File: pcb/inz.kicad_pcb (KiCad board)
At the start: 2 copper layers, 410 parts, among them U1 AMS1117-3.3, U2 ESP32-S3-WROOM-1

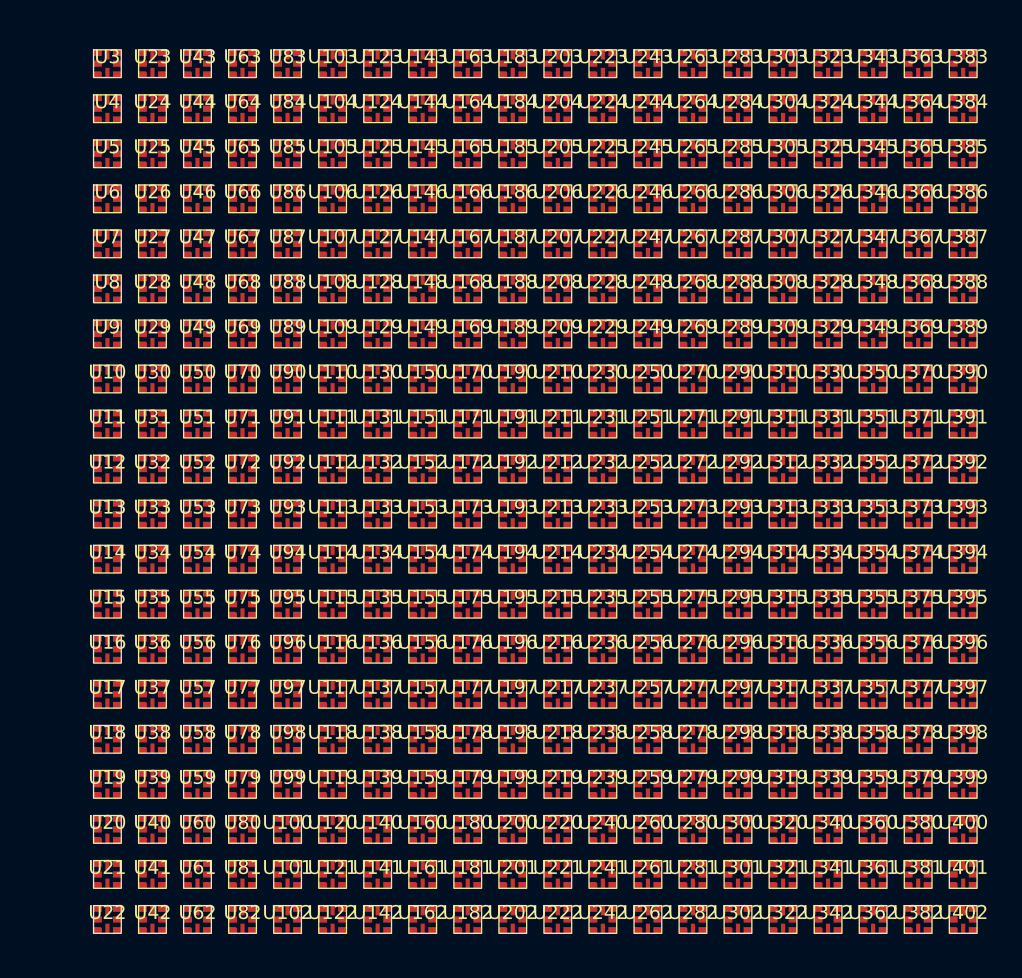
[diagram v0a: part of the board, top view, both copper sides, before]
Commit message: Fixed Led alignment in the pcb project
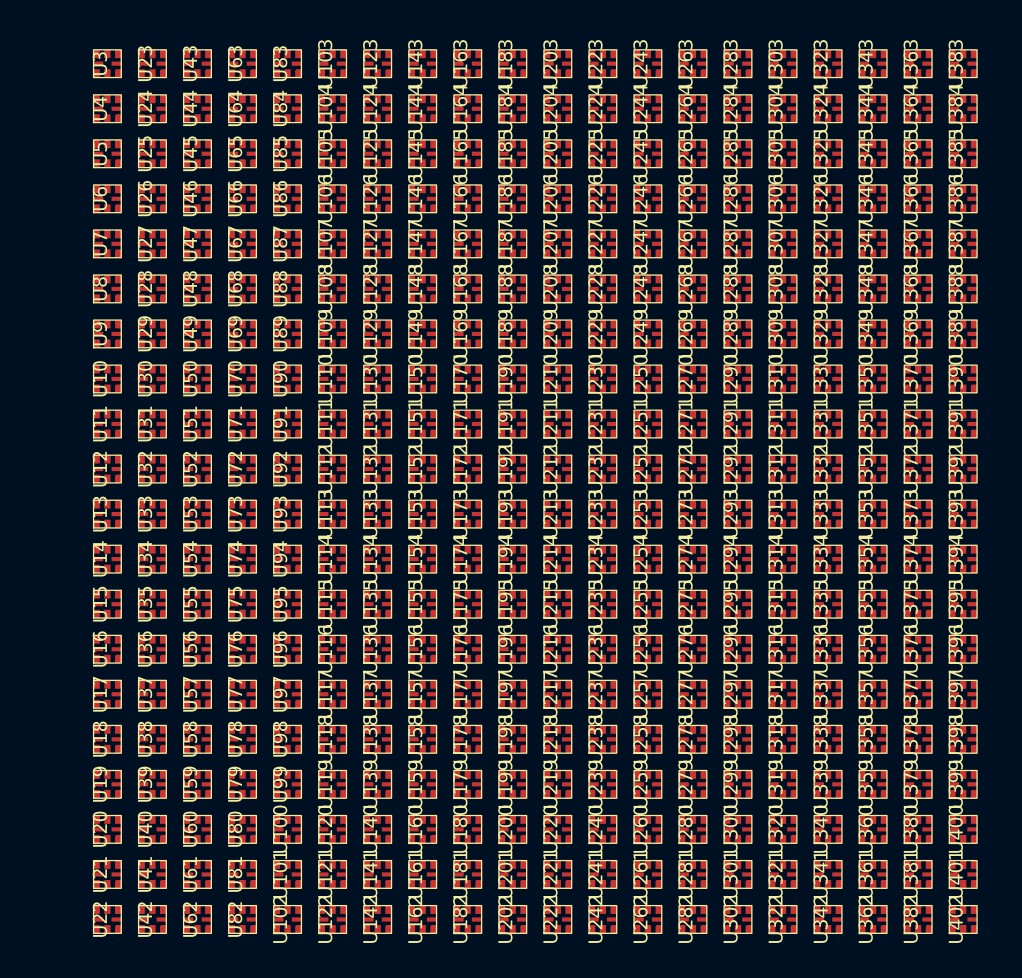
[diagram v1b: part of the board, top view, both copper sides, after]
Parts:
- turned U10 to 90 degrees
- turned U100 to 90 degrees
- turned U101 to 90 degrees
- turned U102 to 90 degrees
- turned U103 to 90 degrees
- turned U104 to 90 degrees
- turned U105 to 90 degrees
- turned U106 to 90 degrees
- turned U107 to 90 degrees
- turned U108 to 90 degrees
- turned U109 to 90 degrees
- turned U11 to 90 degrees
- turned U110 to 90 degrees
- turned U111 to 90 degrees
- turned U112 to 90 degrees
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
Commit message: pcb update
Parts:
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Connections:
- U103 pad 3: Net-(U103-CLI) -> Net-(U102-CLO)
- U103 pad 6: Net-(U103-DAI) -> Net-(U102-DAO)
- U104 pad 1: Net-(U103-CLI) -> Net-(U104-CLO)
- U104 pad 3: Net-(U104-CLI) -> Net-(U103-CLO)
- U104 pad 4: Net-(U103-DAI) -> Net-(U104-DAO)
- U104 pad 6: Net-(U104-DAI) -> Net-(U103-DAO)
- U105 pad 1: Net-(U104-CLI) -> Net-(U105-CLO)
- U105 pad 3: Net-(U105-CLI) -> Net-(U104-CLO)
- U105 pad 4: Net-(U104-DAI) -> Net-(U105-DAO)
- U105 pad 6: Net-(U105-DAI) -> Net-(U104-DAO)
- U106 pad 1: Net-(U105-CLI) -> Net-(U106-CLO)
- U106 pad 3: Net-(U106-CLI) -> Net-(U105-CLO)
- U106 pad 4: Net-(U105-DAI) -> Net-(U106-DAO)
- U106 pad 6: Net-(U106-DAI) -> Net-(U105-DAO)
- U107 pad 1: Net-(U106-CLI) -> Net-(U107-CLO)
- U107 pad 3: Net-(U107-CLI) -> Net-(U106-CLO)
- U107 pad 4: Net-(U106-DAI) -> Net-(U107-DAO)
- U107 pad 6: Net-(U107-DAI) -> Net-(U106-DAO)
- U108 pad 1: Net-(U107-CLI) -> Net-(U108-CLO)
- U108 pad 3: Net-(U108-CLI) -> Net-(U107-CLO)
- U108 pad 4: Net-(U107-DAI) -> Net-(U108-DAO)
- U108 pad 6: Net-(U108-DAI) -> Net-(U107-DAO)
- U109 pad 1: Net-(U108-CLI) -> Net-(U109-CLO)
- U109 pad 3: Net-(U109-CLI) -> Net-(U108-CLO)
- U109 pad 4: Net-(U108-DAI) -> Net-(U109-DAO)
- U109 pad 6: Net-(U109-DAI) -> Net-(U108-DAO)
- U110 pad 1: Net-(U109-CLI) -> Net-(U110-CLO)
- U110 pad 3: Net-(U110-CLI) -> Net-(U109-CLO)
- U110 pad 4: Net-(U109-DAI) -> Net-(U110-DAO)
- U110 pad 6: Net-(U110-DAI) -> Net-(U109-DAO)
- U111 pad 1: Net-(U110-CLI) -> Net-(U111-CLO)
- U111 pad 3: Net-(U111-CLI) -> Net-(U110-CLO)
- U111 pad 4: Net-(U110-DAI) -> Net-(U111-DAO)
- U111 pad 6: Net-(U111-DAI) -> Net-(U110-DAO)
- U112 pad 1: Net-(U111-CLI) -> Net-(U112-CLO)
- U112 pad 3: Net-(U112-CLI) -> Net-(U111-CLO)
- U112 pad 4: Net-(U111-DAI) -> Net-(U112-DAO)
- U112 pad 6: Net-(U112-DAI) -> Net-(U111-DAO)
- U113 pad 1: Net-(U112-CLI) -> Net-(U113-CLO)
- U113 pad 3: Net-(U113-CLI) -> Net-(U112-CLO)
- U113 pad 4: Net-(U112-DAI) -> Net-(U113-DAO)
- U113 pad 6: Net-(U113-DAI) -> Net-(U112-DAO)
- U114 pad 1: Net-(U113-CLI) -> Net-(U114-CLO)
- U114 pad 3: Net-(U114-CLI) -> Net-(U113-CLO)
- U114 pad 4: Net-(U113-DAI) -> Net-(U114-DAO)
- U114 pad 6: Net-(U114-DAI) -> Net-(U113-DAO)
- U115 pad 1: Net-(U114-CLI) -> Net-(U115-CLO)
- U115 pad 3: Net-(U115-CLI) -> Net-(U114-CLO)
- U115 pad 4: Net-(U114-DAI) -> Net-(U115-DAO)
- U115 pad 6: Net-(U115-DAI) -> Net-(U114-DAO)
- U116 pad 1: Net-(U115-CLI) -> Net-(U116-CLO)
- U116 pad 3: Net-(U116-CLI) -> Net-(U115-CLO)
- U116 pad 4: Net-(U115-DAI) -> Net-(U116-DAO)
- U116 pad 6: Net-(U116-DAI) -> Net-(U115-DAO)
- U117 pad 1: Net-(U116-CLI) -> Net-(U117-CLO)
- U117 pad 3: Net-(U117-CLI) -> Net-(U116-CLO)
- U117 pad 4: Net-(U116-DAI) -> Net-(U117-DAO)
- U117 pad 6: Net-(U117-DAI) -> Net-(U116-DAO)
- U118 pad 1: Net-(U117-CLI) -> Net-(U118-CLO)
- U118 pad 3: Net-(U118-CLI) -> Net-(U117-CLO)
- U118 pad 4: Net-(U117-DAI) -> Net-(U118-DAO)
- U118 pad 6: Net-(U118-DAI) -> Net-(U117-DAO)
- U119 pad 1: Net-(U118-CLI) -> Net-(U119-CLO)
- U119 pad 3: Net-(U119-CLI) -> Net-(U118-CLO)
- U119 pad 4: Net-(U118-DAI) -> Net-(U119-DAO)
- U119 pad 6: Net-(U119-DAI) -> Net-(U118-DAO)
- U120 pad 1: Net-(U119-CLI) -> Net-(U120-CLO)
- U120 pad 3: Net-(U120-CLI) -> Net-(U119-CLO)
- U120 pad 4: Net-(U119-DAI) -> Net-(U120-DAO)
- U120 pad 6: Net-(U120-DAI) -> Net-(U119-DAO)
- U121 pad 1: Net-(U120-CLI) -> Net-(U121-CLO)
- U121 pad 3: Net-(U121-CLI) -> Net-(U120-CLO)
- U121 pad 4: Net-(U120-DAI) -> Net-(U121-DAO)
- U121 pad 6: Net-(U121-DAI) -> Net-(U120-DAO)
- U122 pad 1: Net-(U121-CLI) -> Net-(U122-CLO)
- U122 pad 3: Net-(U102-CLO) -> Net-(U121-CLO)
- U122 pad 4: Net-(U121-DAI) -> Net-(U122-DAO)
- U122 pad 6: Net-(U102-DAO) -> Net-(U121-DAO)
- U123 pad 3: Net-(U103-CLO) -> Net-(U122-CLO)
- U123 pad 6: Net-(U103-DAO) -> Net-(U122-DAO)
- U143 pad 3: Net-(U143-CLI) -> Net-(U142-CLO)
- U143 pad 6: Net-(U143-DAI) -> Net-(U142-DAO)
- U144 pad 1: Net-(U143-CLI) -> Net-(U144-CLO)
- U144 pad 3: Net-(U144-CLI) -> Net-(U143-CLO)
- U144 pad 4: Net-(U143-DAI) -> Net-(U144-DAO)
- U144 pad 6: Net-(U144-DAI) -> Net-(U143-DAO)
- U145 pad 1: Net-(U144-CLI) -> Net-(U145-CLO)
- U145 pad 3: Net-(U145-CLI) -> Net-(U144-CLO)
- U145 pad 4: Net-(U144-DAI) -> Net-(U145-DAO)
- U145 pad 6: Net-(U145-DAI) -> Net-(U144-DAO)
- U146 pad 1: Net-(U145-CLI) -> Net-(U146-CLO)
- U146 pad 3: Net-(U146-CLI) -> Net-(U145-CLO)
- U146 pad 4: Net-(U145-DAI) -> Net-(U146-DAO)
- U146 pad 6: Net-(U146-DAI) -> Net-(U145-DAO)
- U147 pad 1: Net-(U146-CLI) -> Net-(U147-CLO)
- U147 pad 3: Net-(U147-CLI) -> Net-(U146-CLO)
- U147 pad 4: Net-(U146-DAI) -> Net-(U147-DAO)
- U147 pad 6: Net-(U147-DAI) -> Net-(U146-DAO)
- U148 pad 1: Net-(U147-CLI) -> Net-(U148-CLO)
- U148 pad 3: Net-(U148-CLI) -> Net-(U147-CLO)
- U148 pad 4: Net-(U147-DAI) -> Net-(U148-DAO)
- U148 pad 6: Net-(U148-DAI) -> Net-(U147-DAO)
- U149 pad 1: Net-(U148-CLI) -> Net-(U149-CLO)
- U149 pad 3: Net-(U149-CLI) -> Net-(U148-CLO)
- U149 pad 4: Net-(U148-DAI) -> Net-(U149-DAO)
- U149 pad 6: Net-(U149-DAI) -> Net-(U148-DAO)
- U150 pad 1: Net-(U149-CLI) -> Net-(U150-CLO)
- U150 pad 3: Net-(U150-CLI) -> Net-(U149-CLO)
- U150 pad 4: Net-(U149-DAI) -> Net-(U150-DAO)
- U150 pad 6: Net-(U150-DAI) -> Net-(U149-DAO)
- U151 pad 1: Net-(U150-CLI) -> Net-(U151-CLO)
- U151 pad 3: Net-(U151-CLI) -> Net-(U150-CLO)
- U151 pad 4: Net-(U150-DAI) -> Net-(U151-DAO)
- U151 pad 6: Net-(U151-DAI) -> Net-(U150-DAO)
- U152 pad 1: Net-(U151-CLI) -> Net-(U152-CLO)
- U152 pad 3: Net-(U152-CLI) -> Net-(U151-CLO)
- U152 pad 4: Net-(U151-DAI) -> Net-(U152-DAO)
- U152 pad 6: Net-(U152-DAI) -> Net-(U151-DAO)
- U153 pad 1: Net-(U152-CLI) -> Net-(U153-CLO)
- U153 pad 3: Net-(U153-CLI) -> Net-(U152-CLO)
- U153 pad 4: Net-(U152-DAI) -> Net-(U153-DAO)
- U153 pad 6: Net-(U153-DAI) -> Net-(U152-DAO)
- U154 pad 1: Net-(U153-CLI) -> Net-(U154-CLO)
- U154 pad 3: Net-(U154-CLI) -> Net-(U153-CLO)
- U154 pad 4: Net-(U153-DAI) -> Net-(U154-DAO)
- U154 pad 6: Net-(U154-DAI) -> Net-(U153-DAO)
- U155 pad 1: Net-(U154-CLI) -> Net-(U155-CLO)
- U155 pad 3: Net-(U155-CLI) -> Net-(U154-CLO)
- U155 pad 4: Net-(U154-DAI) -> Net-(U155-DAO)
- U155 pad 6: Net-(U155-DAI) -> Net-(U154-DAO)
- U156 pad 1: Net-(U155-CLI) -> Net-(U156-CLO)
- U156 pad 3: Net-(U156-CLI) -> Net-(U155-CLO)
- U156 pad 4: Net-(U155-DAI) -> Net-(U156-DAO)
- U156 pad 6: Net-(U156-DAI) -> Net-(U155-DAO)
- U157 pad 1: Net-(U156-CLI) -> Net-(U157-CLO)
- U157 pad 3: Net-(U157-CLI) -> Net-(U156-CLO)
- U157 pad 4: Net-(U156-DAI) -> Net-(U157-DAO)
- U157 pad 6: Net-(U157-DAI) -> Net-(U156-DAO)
- U158 pad 1: Net-(U157-CLI) -> Net-(U158-CLO)
- U158 pad 3: Net-(U158-CLI) -> Net-(U157-CLO)
- U158 pad 4: Net-(U157-DAI) -> Net-(U158-DAO)
- U158 pad 6: Net-(U158-DAI) -> Net-(U157-DAO)
- U159 pad 1: Net-(U158-CLI) -> Net-(U159-CLO)
- U159 pad 3: Net-(U159-CLI) -> Net-(U158-CLO)
- U159 pad 4: Net-(U158-DAI) -> Net-(U159-DAO)
- U159 pad 6: Net-(U159-DAI) -> Net-(U158-DAO)
- U160 pad 1: Net-(U159-CLI) -> Net-(U160-CLO)
- U160 pad 3: Net-(U160-CLI) -> Net-(U159-CLO)
- U160 pad 4: Net-(U159-DAI) -> Net-(U160-DAO)
- U160 pad 6: Net-(U160-DAI) -> Net-(U159-DAO)
- U161 pad 1: Net-(U160-CLI) -> Net-(U161-CLO)
- U161 pad 3: Net-(U161-CLI) -> Net-(U160-CLO)
- U161 pad 4: Net-(U160-DAI) -> Net-(U161-DAO)
- U161 pad 6: Net-(U161-DAI) -> Net-(U160-DAO)
- U162 pad 1: Net-(U161-CLI) -> Net-(U162-CLO)
- U162 pad 3: Net-(U142-CLO) -> Net-(U161-CLO)
- U162 pad 4: Net-(U161-DAI) -> Net-(U162-DAO)
- U162 pad 6: Net-(U142-DAO) -> Net-(U161-DAO)
- U163 pad 3: Net-(U143-CLO) -> Net-(U162-CLO)
- U163 pad 6: Net-(U143-DAO) -> Net-(U162-DAO)
- U183 pad 1: unconnected-(U183-CLO-Pad1) -> Net-(U183-CLO)
- U183 pad 3: Net-(U183-CLI) -> Net-(U182-CLO)
- U183 pad 4: unconnected-(U183-DAO-Pad4) -> Net-(U183-DAO)
- U183 pad 6: Net-(U183-DAI) -> Net-(U182-DAO)
- U184 pad 1: Net-(U183-CLI) -> Net-(U184-CLO)
- U184 pad 3: Net-(U184-CLI) -> Net-(U183-CLO)
- U184 pad 4: Net-(U183-DAI) -> Net-(U184-DAO)
- U184 pad 6: Net-(U184-DAI) -> Net-(U183-DAO)
- U185 pad 1: Net-(U184-CLI) -> Net-(U185-CLO)
- U185 pad 3: Net-(U185-CLI) -> Net-(U184-CLO)
- U185 pad 4: Net-(U184-DAI) -> Net-(U185-DAO)
- U185 pad 6: Net-(U185-DAI) -> Net-(U184-DAO)
- U186 pad 1: Net-(U185-CLI) -> Net-(U186-CLO)
- U186 pad 3: Net-(U186-CLI) -> Net-(U185-CLO)
- U186 pad 4: Net-(U185-DAI) -> Net-(U186-DAO)
- U186 pad 6: Net-(U186-DAI) -> Net-(U185-DAO)
- U187 pad 1: Net-(U186-CLI) -> Net-(U187-CLO)
- U187 pad 3: Net-(U187-CLI) -> Net-(U186-CLO)
- U187 pad 4: Net-(U186-DAI) -> Net-(U187-DAO)
- U187 pad 6: Net-(U187-DAI) -> Net-(U186-DAO)
- U188 pad 1: Net-(U187-CLI) -> Net-(U188-CLO)
- U188 pad 3: Net-(U188-CLI) -> Net-(U187-CLO)
- U188 pad 4: Net-(U187-DAI) -> Net-(U188-DAO)
- U188 pad 6: Net-(U188-DAI) -> Net-(U187-DAO)
- U189 pad 1: Net-(U188-CLI) -> Net-(U189-CLO)
- U189 pad 3: Net-(U189-CLI) -> Net-(U188-CLO)
- U189 pad 4: Net-(U188-DAI) -> Net-(U189-DAO)
- U189 pad 6: Net-(U189-DAI) -> Net-(U188-DAO)
- U190 pad 1: Net-(U189-CLI) -> Net-(U190-CLO)
- U190 pad 3: Net-(U190-CLI) -> Net-(U189-CLO)
- U190 pad 4: Net-(U189-DAI) -> Net-(U190-DAO)
- U190 pad 6: Net-(U190-DAI) -> Net-(U189-DAO)
- U191 pad 1: Net-(U190-CLI) -> Net-(U191-CLO)
- U191 pad 3: Net-(U191-CLI) -> Net-(U190-CLO)
- U191 pad 4: Net-(U190-DAI) -> Net-(U191-DAO)
- U191 pad 6: Net-(U191-DAI) -> Net-(U190-DAO)
- U192 pad 1: Net-(U191-CLI) -> Net-(U192-CLO)
- U192 pad 3: Net-(U192-CLI) -> Net-(U191-CLO)
- U192 pad 4: Net-(U191-DAI) -> Net-(U192-DAO)
- U192 pad 6: Net-(U192-DAI) -> Net-(U191-DAO)
- U193 pad 1: Net-(U192-CLI) -> Net-(U193-CLO)
- U193 pad 3: Net-(U193-CLI) -> Net-(U192-CLO)
- U193 pad 4: Net-(U192-DAI) -> Net-(U193-DAO)
- U193 pad 6: Net-(U193-DAI) -> Net-(U192-DAO)
- U194 pad 1: Net-(U193-CLI) -> Net-(U194-CLO)
- U194 pad 3: Net-(U194-CLI) -> Net-(U193-CLO)
- U194 pad 4: Net-(U193-DAI) -> Net-(U194-DAO)
- U194 pad 6: Net-(U194-DAI) -> Net-(U193-DAO)
- U195 pad 1: Net-(U194-CLI) -> Net-(U195-CLO)
- U195 pad 3: Net-(U195-CLI) -> Net-(U194-CLO)
- U195 pad 4: Net-(U194-DAI) -> Net-(U195-DAO)
- U195 pad 6: Net-(U195-DAI) -> Net-(U194-DAO)
- U196 pad 1: Net-(U195-CLI) -> Net-(U196-CLO)
- U196 pad 3: Net-(U196-CLI) -> Net-(U195-CLO)
- U196 pad 4: Net-(U195-DAI) -> Net-(U196-DAO)
- U196 pad 6: Net-(U196-DAI) -> Net-(U195-DAO)
- U197 pad 1: Net-(U196-CLI) -> Net-(U197-CLO)
- U197 pad 3: Net-(U197-CLI) -> Net-(U196-CLO)
- U197 pad 4: Net-(U196-DAI) -> Net-(U197-DAO)
- U197 pad 6: Net-(U197-DAI) -> Net-(U196-DAO)
- U198 pad 1: Net-(U197-CLI) -> Net-(U198-CLO)
- U198 pad 3: Net-(U198-CLI) -> Net-(U197-CLO)
- U198 pad 4: Net-(U197-DAI) -> Net-(U198-DAO)
- U198 pad 6: Net-(U198-DAI) -> Net-(U197-DAO)
- U199 pad 1: Net-(U198-CLI) -> Net-(U199-CLO)
- U199 pad 3: Net-(U199-CLI) -> Net-(U198-CLO)
- U199 pad 4: Net-(U198-DAI) -> Net-(U199-DAO)
- U199 pad 6: Net-(U199-DAI) -> Net-(U198-DAO)
- U200 pad 1: Net-(U199-CLI) -> Net-(U200-CLO)
- U200 pad 3: Net-(U200-CLI) -> Net-(U199-CLO)
- U200 pad 4: Net-(U199-DAI) -> Net-(U200-DAO)
- U200 pad 6: Net-(U200-DAI) -> Net-(U199-DAO)
- U201 pad 1: Net-(U200-CLI) -> Net-(U201-CLO)
- U201 pad 3: Net-(U201-CLI) -> Net-(U200-CLO)
- U201 pad 4: Net-(U200-DAI) -> Net-(U201-DAO)
- U201 pad 6: Net-(U201-DAI) -> Net-(U200-DAO)
- U202 pad 1: Net-(U201-CLI) -> unconnected-(U202-CLO-Pad1)
- U202 pad 3: Net-(U182-CLO) -> Net-(U201-CLO)
- U202 pad 4: Net-(U201-DAI) -> unconnected-(U202-DAO-Pad4)
- U202 pad 6: Net-(U182-DAO) -> Net-(U201-DAO)
- U223 pad 3: Net-(U223-CLI) -> Net-(U222-CLO)
- U223 pad 6: Net-(U223-DAI) -> Net-(U222-DAO)
- U224 pad 1: Net-(U223-CLI) -> Net-(U224-CLO)
- U224 pad 3: Net-(U224-CLI) -> Net-(U223-CLO)
- U224 pad 4: Net-(U223-DAI) -> Net-(U224-DAO)
- U224 pad 6: Net-(U224-DAI) -> Net-(U223-DAO)
- U225 pad 1: Net-(U224-CLI) -> Net-(U225-CLO)
- U225 pad 3: Net-(U225-CLI) -> Net-(U224-CLO)
- U225 pad 4: Net-(U224-DAI) -> Net-(U225-DAO)
- U225 pad 6: Net-(U225-DAI) -> Net-(U224-DAO)
- U226 pad 1: Net-(U225-CLI) -> Net-(U226-CLO)
- U226 pad 3: Net-(U226-CLI) -> Net-(U225-CLO)
- U226 pad 4: Net-(U225-DAI) -> Net-(U226-DAO)
- U226 pad 6: Net-(U226-DAI) -> Net-(U225-DAO)
- U227 pad 1: Net-(U226-CLI) -> Net-(U227-CLO)
- U227 pad 3: Net-(U227-CLI) -> Net-(U226-CLO)
- U227 pad 4: Net-(U226-DAI) -> Net-(U227-DAO)
- U227 pad 6: Net-(U227-DAI) -> Net-(U226-DAO)
- U228 pad 1: Net-(U227-CLI) -> Net-(U228-CLO)
- U228 pad 3: Net-(U228-CLI) -> Net-(U227-CLO)
- U228 pad 4: Net-(U227-DAI) -> Net-(U228-DAO)
- U228 pad 6: Net-(U228-DAI) -> Net-(U227-DAO)
- U229 pad 1: Net-(U228-CLI) -> Net-(U229-CLO)
- U229 pad 3: Net-(U229-CLI) -> Net-(U228-CLO)
- U229 pad 4: Net-(U228-DAI) -> Net-(U229-DAO)
- U229 pad 6: Net-(U229-DAI) -> Net-(U228-DAO)
- U23 pad 3: Net-(U23-CLI) -> Net-(U22-CLO)
- U23 pad 6: Net-(U23-DAI) -> Net-(U22-DAO)
- U230 pad 1: Net-(U229-CLI) -> Net-(U230-CLO)
- U230 pad 3: Net-(U230-CLI) -> Net-(U229-CLO)
- U230 pad 4: Net-(U229-DAI) -> Net-(U230-DAO)
- U230 pad 6: Net-(U230-DAI) -> Net-(U229-DAO)
- U231 pad 1: Net-(U230-CLI) -> Net-(U231-CLO)
- U231 pad 3: Net-(U231-CLI) -> Net-(U230-CLO)
- U231 pad 4: Net-(U230-DAI) -> Net-(U231-DAO)
- U231 pad 6: Net-(U231-DAI) -> Net-(U230-DAO)
- U232 pad 1: Net-(U231-CLI) -> Net-(U232-CLO)
- U232 pad 3: Net-(U232-CLI) -> Net-(U231-CLO)
- U232 pad 4: Net-(U231-DAI) -> Net-(U232-DAO)
- U232 pad 6: Net-(U232-DAI) -> Net-(U231-DAO)
- U233 pad 1: Net-(U232-CLI) -> Net-(U233-CLO)
- U233 pad 3: Net-(U233-CLI) -> Net-(U232-CLO)
- U233 pad 4: Net-(U232-DAI) -> Net-(U233-DAO)
- U233 pad 6: Net-(U233-DAI) -> Net-(U232-DAO)
- U234 pad 1: Net-(U233-CLI) -> Net-(U234-CLO)
- U234 pad 3: Net-(U234-CLI) -> Net-(U233-CLO)
- U234 pad 4: Net-(U233-DAI) -> Net-(U234-DAO)
- U234 pad 6: Net-(U234-DAI) -> Net-(U233-DAO)
- U235 pad 1: Net-(U234-CLI) -> Net-(U235-CLO)
- U235 pad 3: Net-(U235-CLI) -> Net-(U234-CLO)
- U235 pad 4: Net-(U234-DAI) -> Net-(U235-DAO)
- U235 pad 6: Net-(U235-DAI) -> Net-(U234-DAO)
- U236 pad 1: Net-(U235-CLI) -> Net-(U236-CLO)
- U236 pad 3: Net-(U236-CLI) -> Net-(U235-CLO)
- U236 pad 4: Net-(U235-DAI) -> Net-(U236-DAO)
- U236 pad 6: Net-(U236-DAI) -> Net-(U235-DAO)
- U237 pad 1: Net-(U236-CLI) -> Net-(U237-CLO)
- U237 pad 3: Net-(U237-CLI) -> Net-(U236-CLO)
- U237 pad 4: Net-(U236-DAI) -> Net-(U237-DAO)
- U237 pad 6: Net-(U237-DAI) -> Net-(U236-DAO)
- U238 pad 1: Net-(U237-CLI) -> Net-(U238-CLO)
- U238 pad 3: Net-(U238-CLI) -> Net-(U237-CLO)
- U238 pad 4: Net-(U237-DAI) -> Net-(U238-DAO)
- U238 pad 6: Net-(U238-DAI) -> Net-(U237-DAO)
- U239 pad 1: Net-(U238-CLI) -> Net-(U239-CLO)
- U239 pad 3: Net-(U239-CLI) -> Net-(U238-CLO)
- U239 pad 4: Net-(U238-DAI) -> Net-(U239-DAO)
- U239 pad 6: Net-(U239-DAI) -> Net-(U238-DAO)
- U24 pad 1: Net-(U23-CLI) -> Net-(U24-CLO)
- U24 pad 3: Net-(U24-CLI) -> Net-(U23-CLO)
- U24 pad 4: Net-(U23-DAI) -> Net-(U24-DAO)
- U24 pad 6: Net-(U24-DAI) -> Net-(U23-DAO)
- U240 pad 1: Net-(U239-CLI) -> Net-(U240-CLO)
- U240 pad 3: Net-(U240-CLI) -> Net-(U239-CLO)
- U240 pad 4: Net-(U239-DAI) -> Net-(U240-DAO)
- U240 pad 6: Net-(U240-DAI) -> Net-(U239-DAO)
- U241 pad 1: Net-(U240-CLI) -> Net-(U241-CLO)
- U241 pad 3: Net-(U241-CLI) -> Net-(U240-CLO)
- U241 pad 4: Net-(U240-DAI) -> Net-(U241-DAO)
- U241 pad 6: Net-(U241-DAI) -> Net-(U240-DAO)
- U242 pad 1: Net-(U241-CLI) -> Net-(U242-CLO)
- U242 pad 3: Net-(U222-CLO) -> Net-(U241-CLO)
- U242 pad 4: Net-(U241-DAI) -> Net-(U242-DAO)
- U242 pad 6: Net-(U222-DAO) -> Net-(U241-DAO)
- U243 pad 3: Net-(U223-CLO) -> Net-(U242-CLO)
- U243 pad 6: Net-(U223-DAO) -> Net-(U242-DAO)
- U25 pad 1: Net-(U24-CLI) -> Net-(U25-CLO)
- U25 pad 3: Net-(U25-CLI) -> Net-(U24-CLO)
- U25 pad 4: Net-(U24-DAI) -> Net-(U25-DAO)
- U25 pad 6: Net-(U25-DAI) -> Net-(U24-DAO)
- U26 pad 1: Net-(U25-CLI) -> Net-(U26-CLO)
- U26 pad 3: Net-(U26-CLI) -> Net-(U25-CLO)
- U26 pad 4: Net-(U25-DAI) -> Net-(U26-DAO)
- U26 pad 6: Net-(U26-DAI) -> Net-(U25-DAO)
- U263 pad 3: Net-(U263-CLI) -> Net-(U262-CLO)
- U263 pad 6: Net-(U263-DAI) -> Net-(U262-DAO)
- U264 pad 1: Net-(U263-CLI) -> Net-(U264-CLO)
- U264 pad 3: Net-(U264-CLI) -> Net-(U263-CLO)
- U264 pad 4: Net-(U263-DAI) -> Net-(U264-DAO)
- U264 pad 6: Net-(U264-DAI) -> Net-(U263-DAO)
- U265 pad 1: Net-(U264-CLI) -> Net-(U265-CLO)
- U265 pad 3: Net-(U265-CLI) -> Net-(U264-CLO)
- U265 pad 4: Net-(U264-DAI) -> Net-(U265-DAO)
- U265 pad 6: Net-(U265-DAI) -> Net-(U264-DAO)
- U266 pad 1: Net-(U265-CLI) -> Net-(U266-CLO)
- U266 pad 3: Net-(U266-CLI) -> Net-(U265-CLO)
- U266 pad 4: Net-(U265-DAI) -> Net-(U266-DAO)
- U266 pad 6: Net-(U266-DAI) -> Net-(U265-DAO)
- U267 pad 1: Net-(U266-CLI) -> Net-(U267-CLO)
- U267 pad 3: Net-(U267-CLI) -> Net-(U266-CLO)
- U267 pad 4: Net-(U266-DAI) -> Net-(U267-DAO)
- U267 pad 6: Net-(U267-DAI) -> Net-(U266-DAO)
- U268 pad 1: Net-(U267-CLI) -> Net-(U268-CLO)
- U268 pad 3: Net-(U268-CLI) -> Net-(U267-CLO)
- U268 pad 4: Net-(U267-DAI) -> Net-(U268-DAO)
- U268 pad 6: Net-(U268-DAI) -> Net-(U267-DAO)
- U269 pad 1: Net-(U268-CLI) -> Net-(U269-CLO)
- U269 pad 3: Net-(U269-CLI) -> Net-(U268-CLO)
- U269 pad 4: Net-(U268-DAI) -> Net-(U269-DAO)
- U269 pad 6: Net-(U269-DAI) -> Net-(U268-DAO)
- U27 pad 1: Net-(U26-CLI) -> Net-(U27-CLO)
- U27 pad 3: Net-(U27-CLI) -> Net-(U26-CLO)
- U27 pad 4: Net-(U26-DAI) -> Net-(U27-DAO)
- U27 pad 6: Net-(U27-DAI) -> Net-(U26-DAO)
- U270 pad 1: Net-(U269-CLI) -> Net-(U270-CLO)
- U270 pad 3: Net-(U270-CLI) -> Net-(U269-CLO)
- U270 pad 4: Net-(U269-DAI) -> Net-(U270-DAO)
- U270 pad 6: Net-(U270-DAI) -> Net-(U269-DAO)
- U271 pad 1: Net-(U270-CLI) -> Net-(U271-CLO)
- U271 pad 3: Net-(U271-CLI) -> Net-(U270-CLO)
- U271 pad 4: Net-(U270-DAI) -> Net-(U271-DAO)
- U271 pad 6: Net-(U271-DAI) -> Net-(U270-DAO)
- U272 pad 1: Net-(U271-CLI) -> Net-(U272-CLO)
- U272 pad 3: Net-(U272-CLI) -> Net-(U271-CLO)
- U272 pad 4: Net-(U271-DAI) -> Net-(U272-DAO)
- U272 pad 6: Net-(U272-DAI) -> Net-(U271-DAO)
- U273 pad 1: Net-(U272-CLI) -> Net-(U273-CLO)
- U273 pad 3: Net-(U273-CLI) -> Net-(U272-CLO)
- U273 pad 4: Net-(U272-DAI) -> Net-(U273-DAO)
- U273 pad 6: Net-(U273-DAI) -> Net-(U272-DAO)
- U274 pad 1: Net-(U273-CLI) -> Net-(U274-CLO)
- U274 pad 3: Net-(U274-CLI) -> Net-(U273-CLO)
- U274 pad 4: Net-(U273-DAI) -> Net-(U274-DAO)
- U274 pad 6: Net-(U274-DAI) -> Net-(U273-DAO)
- U275 pad 1: Net-(U274-CLI) -> Net-(U275-CLO)
- U275 pad 3: Net-(U275-CLI) -> Net-(U274-CLO)
- U275 pad 4: Net-(U274-DAI) -> Net-(U275-DAO)
- U275 pad 6: Net-(U275-DAI) -> Net-(U274-DAO)
- U276 pad 1: Net-(U275-CLI) -> Net-(U276-CLO)
- U276 pad 3: Net-(U276-CLI) -> Net-(U275-CLO)
- U276 pad 4: Net-(U275-DAI) -> Net-(U276-DAO)
- U276 pad 6: Net-(U276-DAI) -> Net-(U275-DAO)
- U277 pad 1: Net-(U276-CLI) -> Net-(U277-CLO)
- U277 pad 3: Net-(U277-CLI) -> Net-(U276-CLO)
- U277 pad 4: Net-(U276-DAI) -> Net-(U277-DAO)
- U277 pad 6: Net-(U277-DAI) -> Net-(U276-DAO)
- U278 pad 1: Net-(U277-CLI) -> Net-(U278-CLO)
- U278 pad 3: Net-(U278-CLI) -> Net-(U277-CLO)
- U278 pad 4: Net-(U277-DAI) -> Net-(U278-DAO)
- U278 pad 6: Net-(U278-DAI) -> Net-(U277-DAO)
- U279 pad 1: Net-(U278-CLI) -> Net-(U279-CLO)
- U279 pad 3: Net-(U279-CLI) -> Net-(U278-CLO)
- U279 pad 4: Net-(U278-DAI) -> Net-(U279-DAO)
- U279 pad 6: Net-(U279-DAI) -> Net-(U278-DAO)
- U28 pad 1: Net-(U27-CLI) -> Net-(U28-CLO)
- U28 pad 3: Net-(U28-CLI) -> Net-(U27-CLO)
- U28 pad 4: Net-(U27-DAI) -> Net-(U28-DAO)
- U28 pad 6: Net-(U28-DAI) -> Net-(U27-DAO)
- U280 pad 1: Net-(U279-CLI) -> Net-(U280-CLO)
- U280 pad 3: Net-(U280-CLI) -> Net-(U279-CLO)
- U280 pad 4: Net-(U279-DAI) -> Net-(U280-DAO)
- U280 pad 6: Net-(U280-DAI) -> Net-(U279-DAO)
- U281 pad 1: Net-(U280-CLI) -> Net-(U281-CLO)
- U281 pad 3: Net-(U281-CLI) -> Net-(U280-CLO)
- U281 pad 4: Net-(U280-DAI) -> Net-(U281-DAO)
- U281 pad 6: Net-(U281-DAI) -> Net-(U280-DAO)
- U282 pad 1: Net-(U281-CLI) -> Net-(U282-CLO)
- U282 pad 3: Net-(U262-CLO) -> Net-(U281-CLO)
- U282 pad 4: Net-(U281-DAI) -> Net-(U282-DAO)
- U282 pad 6: Net-(U262-DAO) -> Net-(U281-DAO)
- U283 pad 3: Net-(U263-CLO) -> Net-(U282-CLO)
- U283 pad 6: Net-(U263-DAO) -> Net-(U282-DAO)
- U29 pad 1: Net-(U28-CLI) -> Net-(U29-CLO)
- U29 pad 3: Net-(U29-CLI) -> Net-(U28-CLO)
- U29 pad 4: Net-(U28-DAI) -> Net-(U29-DAO)
- U29 pad 6: Net-(U29-DAI) -> Net-(U28-DAO)
- U30 pad 1: Net-(U29-CLI) -> Net-(U30-CLO)
- U30 pad 3: Net-(U30-CLI) -> Net-(U29-CLO)
- U30 pad 4: Net-(U29-DAI) -> Net-(U30-DAO)
- U30 pad 6: Net-(U30-DAI) -> Net-(U29-DAO)
- U303 pad 3: Net-(U303-CLI) -> Net-(U302-CLO)
- U303 pad 6: Net-(U303-DAI) -> Net-(U302-DAO)
- U304 pad 1: Net-(U303-CLI) -> Net-(U304-CLO)
- U304 pad 3: Net-(U304-CLI) -> Net-(U303-CLO)
- U304 pad 4: Net-(U303-DAI) -> Net-(U304-DAO)
- U304 pad 6: Net-(U304-DAI) -> Net-(U303-DAO)
- U305 pad 1: Net-(U304-CLI) -> Net-(U305-CLO)
- U305 pad 3: Net-(U305-CLI) -> Net-(U304-CLO)
- U305 pad 4: Net-(U304-DAI) -> Net-(U305-DAO)
- U305 pad 6: Net-(U305-DAI) -> Net-(U304-DAO)
- U306 pad 1: Net-(U305-CLI) -> Net-(U306-CLO)
- U306 pad 3: Net-(U306-CLI) -> Net-(U305-CLO)
- U306 pad 4: Net-(U305-DAI) -> Net-(U306-DAO)
- U306 pad 6: Net-(U306-DAI) -> Net-(U305-DAO)
- U307 pad 1: Net-(U306-CLI) -> Net-(U307-CLO)
- U307 pad 3: Net-(U307-CLI) -> Net-(U306-CLO)
- U307 pad 4: Net-(U306-DAI) -> Net-(U307-DAO)
- U307 pad 6: Net-(U307-DAI) -> Net-(U306-DAO)
- U308 pad 1: Net-(U307-CLI) -> Net-(U308-CLO)
- U308 pad 3: Net-(U308-CLI) -> Net-(U307-CLO)
- U308 pad 4: Net-(U307-DAI) -> Net-(U308-DAO)
- U308 pad 6: Net-(U308-DAI) -> Net-(U307-DAO)
- U309 pad 1: Net-(U308-CLI) -> Net-(U309-CLO)
- U309 pad 3: Net-(U309-CLI) -> Net-(U308-CLO)
- U309 pad 4: Net-(U308-DAI) -> Net-(U309-DAO)
- U309 pad 6: Net-(U309-DAI) -> Net-(U308-DAO)
- U31 pad 1: Net-(U30-CLI) -> Net-(U31-CLO)
- U31 pad 3: Net-(U31-CLI) -> Net-(U30-CLO)
- U31 pad 4: Net-(U30-DAI) -> Net-(U31-DAO)
- U31 pad 6: Net-(U31-DAI) -> Net-(U30-DAO)
- U310 pad 1: Net-(U309-CLI) -> Net-(U310-CLO)
- U310 pad 3: Net-(U310-CLI) -> Net-(U309-CLO)
- U310 pad 4: Net-(U309-DAI) -> Net-(U310-DAO)
- U310 pad 6: Net-(U310-DAI) -> Net-(U309-DAO)
- U311 pad 1: Net-(U310-CLI) -> Net-(U311-CLO)
- U311 pad 3: Net-(U311-CLI) -> Net-(U310-CLO)
- U311 pad 4: Net-(U310-DAI) -> Net-(U311-DAO)
- U311 pad 6: Net-(U311-DAI) -> Net-(U310-DAO)
- U312 pad 1: Net-(U311-CLI) -> Net-(U312-CLO)
- U312 pad 3: Net-(U312-CLI) -> Net-(U311-CLO)
- U312 pad 4: Net-(U311-DAI) -> Net-(U312-DAO)
- U312 pad 6: Net-(U312-DAI) -> Net-(U311-DAO)
- U313 pad 1: Net-(U312-CLI) -> Net-(U313-CLO)
- U313 pad 3: Net-(U313-CLI) -> Net-(U312-CLO)
- U313 pad 4: Net-(U312-DAI) -> Net-(U313-DAO)
- U313 pad 6: Net-(U313-DAI) -> Net-(U312-DAO)
- U314 pad 1: Net-(U313-CLI) -> Net-(U314-CLO)
- U314 pad 3: Net-(U314-CLI) -> Net-(U313-CLO)
- U314 pad 4: Net-(U313-DAI) -> Net-(U314-DAO)
- U314 pad 6: Net-(U314-DAI) -> Net-(U313-DAO)
- U315 pad 1: Net-(U314-CLI) -> Net-(U315-CLO)
- U315 pad 3: Net-(U315-CLI) -> Net-(U314-CLO)
- U315 pad 4: Net-(U314-DAI) -> Net-(U315-DAO)
- U315 pad 6: Net-(U315-DAI) -> Net-(U314-DAO)
- U316 pad 1: Net-(U315-CLI) -> Net-(U316-CLO)
- U316 pad 3: Net-(U316-CLI) -> Net-(U315-CLO)
- U316 pad 4: Net-(U315-DAI) -> Net-(U316-DAO)
- U316 pad 6: Net-(U316-DAI) -> Net-(U315-DAO)
- U317 pad 1: Net-(U316-CLI) -> Net-(U317-CLO)
- U317 pad 3: Net-(U317-CLI) -> Net-(U316-CLO)
- U317 pad 4: Net-(U316-DAI) -> Net-(U317-DAO)
- U317 pad 6: Net-(U317-DAI) -> Net-(U316-DAO)
- U318 pad 1: Net-(U317-CLI) -> Net-(U318-CLO)
- U318 pad 3: Net-(U318-CLI) -> Net-(U317-CLO)
- U318 pad 4: Net-(U317-DAI) -> Net-(U318-DAO)
- U318 pad 6: Net-(U318-DAI) -> Net-(U317-DAO)
- U319 pad 1: Net-(U318-CLI) -> Net-(U319-CLO)
- U319 pad 3: Net-(U319-CLI) -> Net-(U318-CLO)
- U319 pad 4: Net-(U318-DAI) -> Net-(U319-DAO)
- U319 pad 6: Net-(U319-DAI) -> Net-(U318-DAO)
- U32 pad 1: Net-(U31-CLI) -> Net-(U32-CLO)
- U32 pad 3: Net-(U32-CLI) -> Net-(U31-CLO)
- U32 pad 4: Net-(U31-DAI) -> Net-(U32-DAO)
- U32 pad 6: Net-(U32-DAI) -> Net-(U31-DAO)
- U320 pad 1: Net-(U319-CLI) -> Net-(U320-CLO)
- U320 pad 3: Net-(U320-CLI) -> Net-(U319-CLO)
- U320 pad 4: Net-(U319-DAI) -> Net-(U320-DAO)
- U320 pad 6: Net-(U320-DAI) -> Net-(U319-DAO)
- U321 pad 1: Net-(U320-CLI) -> Net-(U321-CLO)
- U321 pad 3: Net-(U321-CLI) -> Net-(U320-CLO)
- U321 pad 4: Net-(U320-DAI) -> Net-(U321-DAO)
- U321 pad 6: Net-(U321-DAI) -> Net-(U320-DAO)
- U322 pad 1: Net-(U321-CLI) -> Net-(U322-CLO)
- U322 pad 3: Net-(U302-CLO) -> Net-(U321-CLO)
- U322 pad 4: Net-(U321-DAI) -> Net-(U322-DAO)
- U322 pad 6: Net-(U302-DAO) -> Net-(U321-DAO)
- U323 pad 3: Net-(U303-CLO) -> Net-(U322-CLO)
- U323 pad 6: Net-(U303-DAO) -> Net-(U322-DAO)
- U33 pad 1: Net-(U32-CLI) -> Net-(U33-CLO)
- U33 pad 3: Net-(U33-CLI) -> Net-(U32-CLO)
- U33 pad 4: Net-(U32-DAI) -> Net-(U33-DAO)
- U33 pad 6: Net-(U33-DAI) -> Net-(U32-DAO)
- U34 pad 1: Net-(U33-CLI) -> Net-(U34-CLO)
- U34 pad 3: Net-(U34-CLI) -> Net-(U33-CLO)
- U34 pad 4: Net-(U33-DAI) -> Net-(U34-DAO)
- U34 pad 6: Net-(U34-DAI) -> Net-(U33-DAO)
- U343 pad 3: Net-(U343-CLI) -> Net-(U342-CLO)
- U343 pad 6: Net-(U343-DAI) -> Net-(U342-DAO)
- U344 pad 1: Net-(U343-CLI) -> Net-(U344-CLO)
- U344 pad 3: Net-(U344-CLI) -> Net-(U343-CLO)
- U344 pad 4: Net-(U343-DAI) -> Net-(U344-DAO)
- U344 pad 6: Net-(U344-DAI) -> Net-(U343-DAO)
- U345 pad 1: Net-(U344-CLI) -> Net-(U345-CLO)
- U345 pad 3: Net-(U345-CLI) -> Net-(U344-CLO)
- U345 pad 4: Net-(U344-DAI) -> Net-(U345-DAO)
- U345 pad 6: Net-(U345-DAI) -> Net-(U344-DAO)
- U346 pad 1: Net-(U345-CLI) -> Net-(U346-CLO)
- U346 pad 3: Net-(U346-CLI) -> Net-(U345-CLO)
- U346 pad 4: Net-(U345-DAI) -> Net-(U346-DAO)
- U346 pad 6: Net-(U346-DAI) -> Net-(U345-DAO)
- U347 pad 1: Net-(U346-CLI) -> Net-(U347-CLO)
- U347 pad 3: Net-(U347-CLI) -> Net-(U346-CLO)
- U347 pad 4: Net-(U346-DAI) -> Net-(U347-DAO)
- U347 pad 6: Net-(U347-DAI) -> Net-(U346-DAO)
- U348 pad 1: Net-(U347-CLI) -> Net-(U348-CLO)
- U348 pad 3: Net-(U348-CLI) -> Net-(U347-CLO)
- U348 pad 4: Net-(U347-DAI) -> Net-(U348-DAO)
- U348 pad 6: Net-(U348-DAI) -> Net-(U347-DAO)
- U349 pad 1: Net-(U348-CLI) -> Net-(U349-CLO)
- U349 pad 3: Net-(U349-CLI) -> Net-(U348-CLO)
- U349 pad 4: Net-(U348-DAI) -> Net-(U349-DAO)
- U349 pad 6: Net-(U349-DAI) -> Net-(U348-DAO)
- U35 pad 1: Net-(U34-CLI) -> Net-(U35-CLO)
- U35 pad 3: Net-(U35-CLI) -> Net-(U34-CLO)
- U35 pad 4: Net-(U34-DAI) -> Net-(U35-DAO)
- U35 pad 6: Net-(U35-DAI) -> Net-(U34-DAO)
- U350 pad 1: Net-(U349-CLI) -> Net-(U350-CLO)
- U350 pad 3: Net-(U350-CLI) -> Net-(U349-CLO)
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
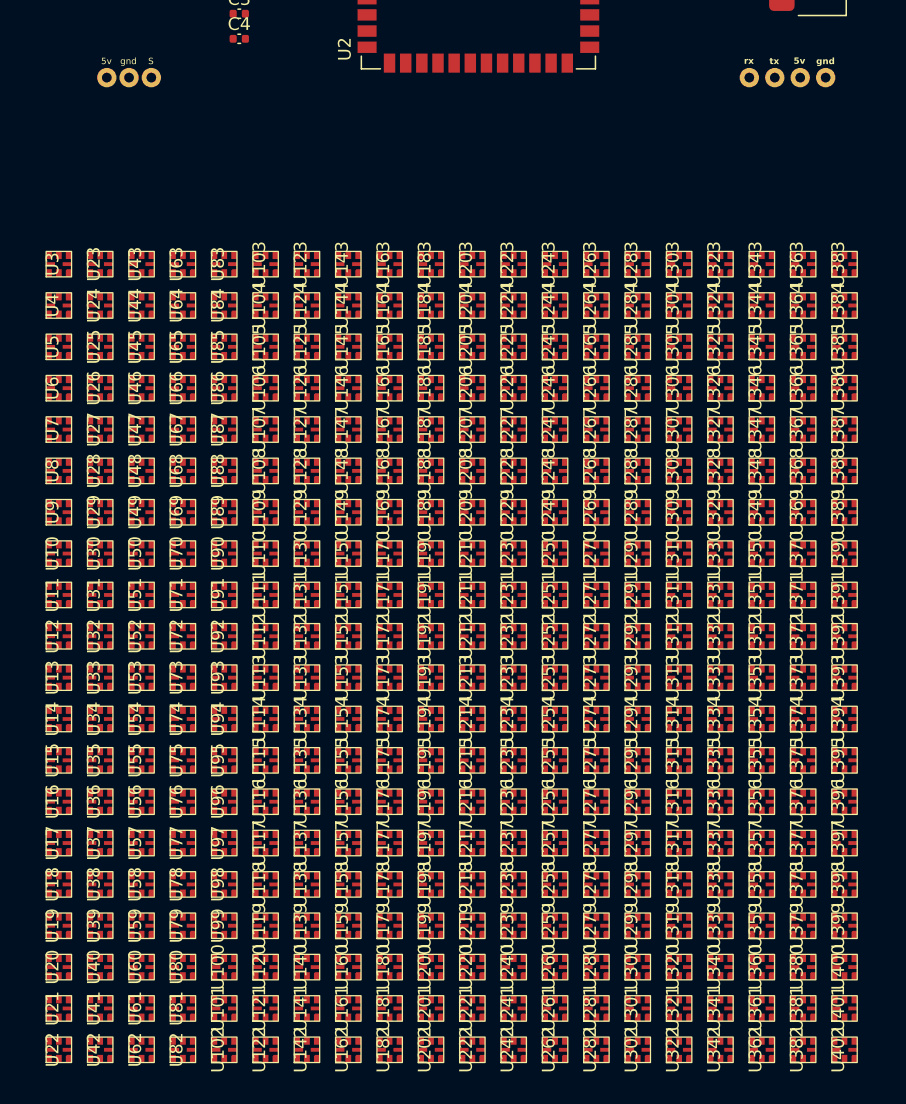
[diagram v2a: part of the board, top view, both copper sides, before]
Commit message: Added led connections on pcb
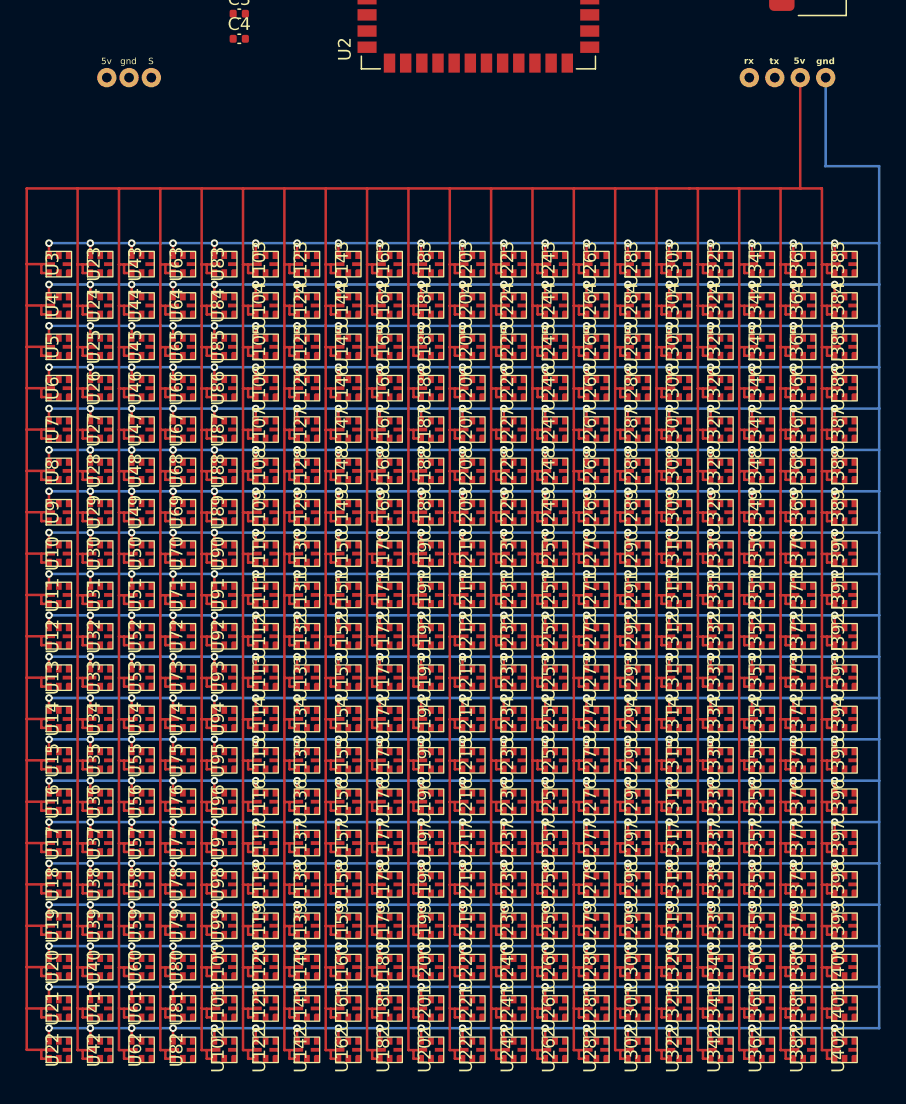
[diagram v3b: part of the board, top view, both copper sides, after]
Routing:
- net +5V: track 0.00 -> 2399.6 mm
- net GND: track 0.00 -> 1784.0 mm, vias 0 -> 400

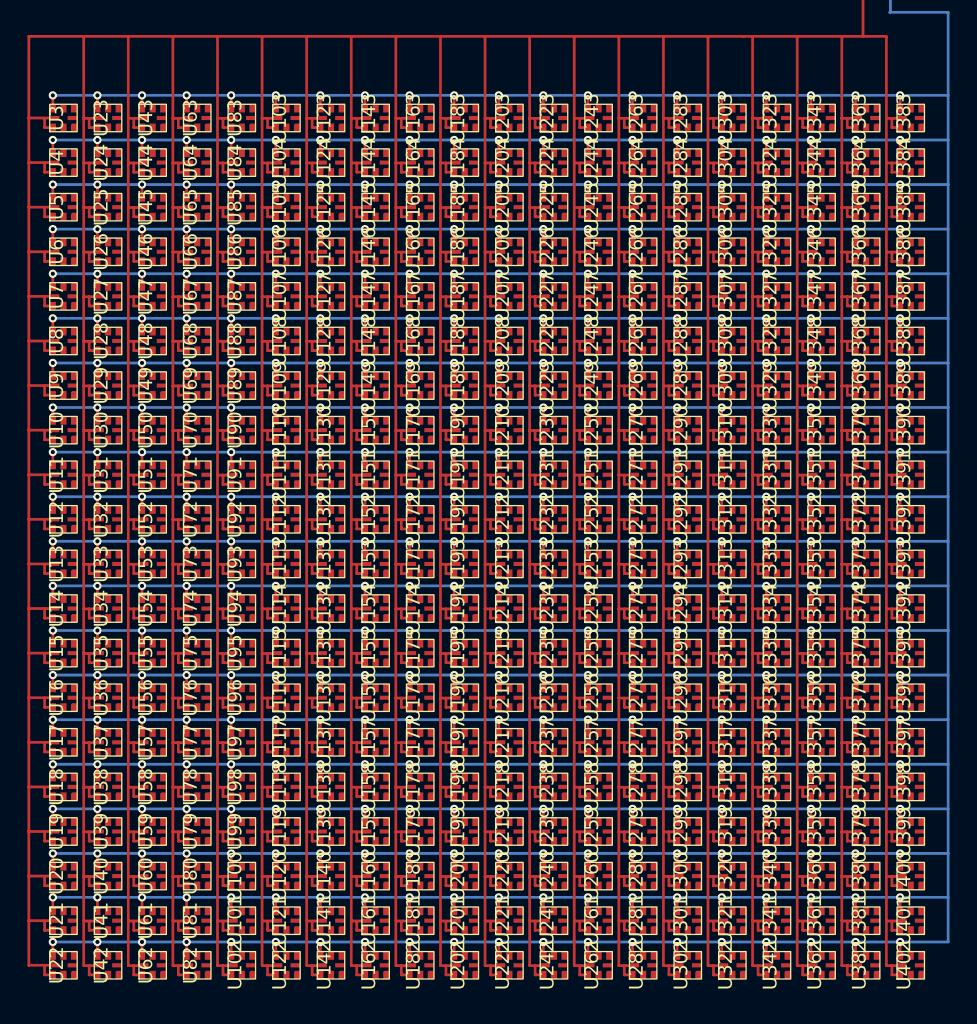
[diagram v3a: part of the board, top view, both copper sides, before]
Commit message: Connected led columns together
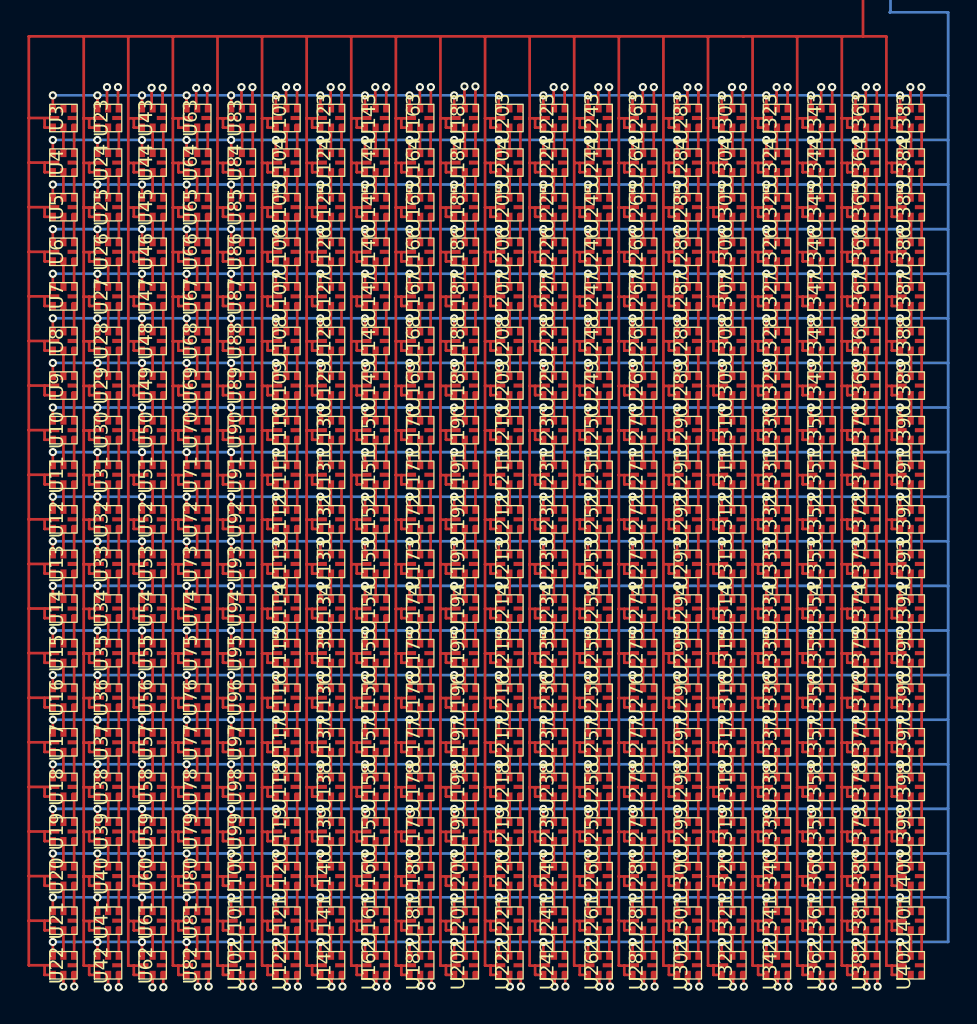
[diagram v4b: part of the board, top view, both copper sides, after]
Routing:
- net Net-(U22-CLO): track 0.00 -> 70.2 mm, vias 0 -> 2
- net Net-(U62-CLO): track 0.00 -> 70.0 mm, vias 0 -> 2
- net Net-(U42-CLO): track 0.00 -> 70.0 mm, vias 0 -> 2
- net Net-(U182-CLO): track 0.00 -> 70.0 mm, vias 0 -> 2
- net Net-(U82-CLO): track 0.00 -> 70.0 mm, vias 0 -> 2
- net Net-(U282-CLO): track 0.00 -> 70.0 mm, vias 0 -> 2
- net Net-(U262-CLO): track 0.00 -> 70.0 mm, vias 0 -> 2
- net Net-(U242-CLO): track 0.00 -> 70.0 mm, vias 0 -> 2
- net Net-(U222-CLO): track 0.00 -> 70.0 mm, vias 0 -> 2
- net Net-(U162-CLO): track 0.00 -> 70.0 mm, vias 0 -> 2
- net Net-(U142-CLO): track 0.00 -> 70.0 mm, vias 0 -> 2
- net Net-(U122-CLO): track 0.00 -> 70.0 mm, vias 0 -> 2
- net Net-(U102-CLO): track 0.00 -> 70.0 mm, vias 0 -> 2
- net Net-(U382-CLO): track 0.00 -> 70.0 mm, vias 0 -> 2
- net Net-(U362-CLO): track 0.00 -> 70.0 mm, vias 0 -> 2
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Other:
- copper layers 2 -> 4

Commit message: +feat: finished second pcb design
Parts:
- removed JT1: ~, LED_SMD:UART JT
- added LED_CON1: ~, RF_Module:led_con, F.Cu at (145.8, 132.6)
- added LED_CON2: ~, RF_Module:led_con, F.Cu at (145.8, 138.6)
- added pwr1: ~, RF_Module:5vgnd, F.Cu at (119.0, 148.0)
- added pwr2: ~, RF_Module:5vgnd, F.Cu at (122.0, 49.0)
- added rxtx1: ~, RF_Module:rxtx, F.Cu at (97.7, 132.3)
- C1, C2, C3, C4, R1, ST1, U1, U2: moved to B.Cu
- moved U22 122.8 mm to (153.4, 60.1), turned to -90 degrees
- moved U42 119.2 mm to (150.2, 60.1), turned to -90 degrees
- moved U21 117.5 mm to (153.4, 63.4), turned to -90 degrees
- moved U62 115.8 mm to (146.9, 60.1), turned to -90 degrees
- moved U402 113.8 mm to (91.7, 60.1), turned to -90 degrees
- moved U41 113.7 mm to (150.2, 63.4), turned to -90 degrees
- moved U82 112.7 mm to (143.7, 60.1), turned to -90 degrees
- moved U20 112.4 mm to (153.4, 66.6), turned to -90 degrees
- moved U382 110.9 mm to (94.9, 60.1), turned to -90 degrees
- moved U61 110.2 mm to (146.9, 63.4), turned to -90 degrees
- moved U102 110.0 mm to (140.4, 60.1), turned to -90 degrees
- moved U40 108.4 mm to (150.2, 66.6), turned to -90 degrees
- moved U362 108.3 mm to (98.2, 60.1), turned to -90 degrees
- moved U401 108.0 mm to (91.7, 63.4), turned to -90 degrees
- moved U122 107.5 mm to (137.2, 60.1), turned to -90 degrees
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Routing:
- net GND: track 1784.0 -> 1926.3 mm, vias 400 -> 386
- net +5V: track 2399.6 -> 2539.1 mm, vias 0 -> 4
- net Net-(LED_CON2-cli): track 0.00 -> 57.7 mm, vias 0 -> 2
- net Net-(LED_CON2-dai): track 0.00 -> 48.0 mm, vias 0 -> 2
- net Net-(LED_CON1-cli): track 0.00 -> 42.2 mm, vias 0 -> 1
- net Net-(LED_CON1-dai): track 0.00 -> 41.0 mm, vias 0 -> 1
- net Net-(U1-VO): track 0.00 -> 38.5 mm, vias 0 -> 2
- net UART_TX: track 0.00 -> 34.5 mm, vias 0 -> 2
- net UART_RX: track 0.00 -> 28.7 mm, vias 0 -> 2
- net Net-(JT2-S): track 0.00 -> 20.1 mm, vias 0 -> 2
- net Net-(U2-IO0): track 0.00 -> 11.5 mm
- net Net-(U2-EN): track 0.00 -> 2.70 mm
- net Net-(U382-CLO): track 70.0 -> 71.4 mm
- net Net-(U362-CLO): track 70.0 -> 71.4 mm
- net Net-(U342-CLO): track 70.0 -> 71.4 mm
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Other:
- board outline added: 66 x 117 mm
